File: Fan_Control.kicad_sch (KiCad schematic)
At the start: 6 parts, among them J20 Conn_01x03, J21 Conn_01x03

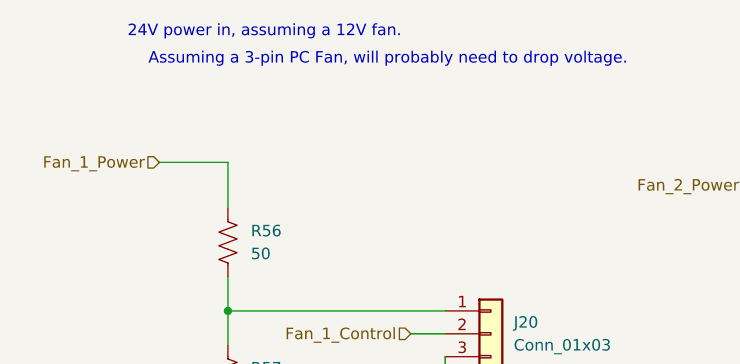
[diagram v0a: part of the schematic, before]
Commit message: Updated most of root-page labels.
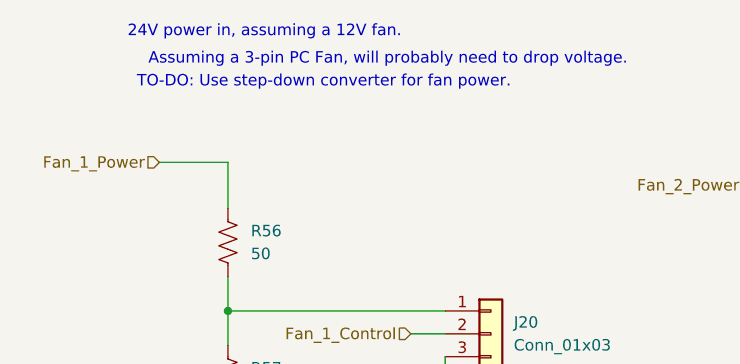
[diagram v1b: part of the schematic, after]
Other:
- note added: "TO-DO: Use step-down converter for fan power."
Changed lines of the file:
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@@
+		)
+	)
+	(text "TO-DO: Use step-down converter for fan power."
+		(exclude_from_sim no)
+		(at 67.818 82.55 0)
+		(effects
+			(font
+				(size 1.27 1.27)
+			)
 		)
 	)

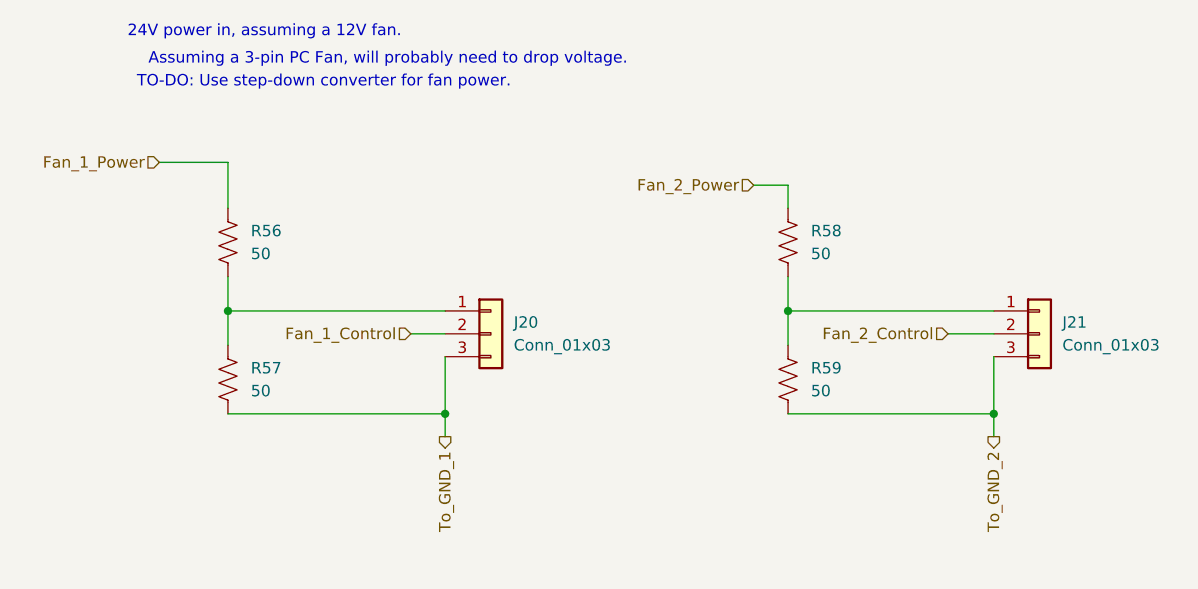
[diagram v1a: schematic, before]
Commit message: Added 24V-12V step-down converter for fans, started switch to devkit.
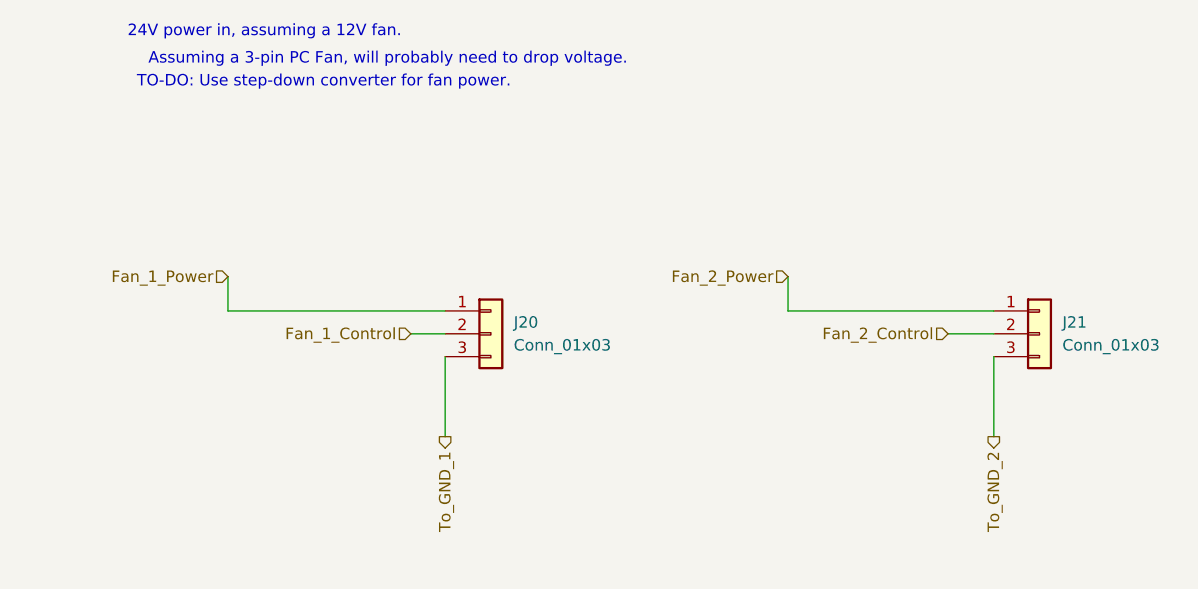
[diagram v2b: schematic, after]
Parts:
- removed R56, R57, R58, R59: 50, symbol Device:R_US
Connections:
- net Fan_1_Power: now also J20.1 (Pin_1)
- net Fan_2_Power: now also J21.1 (Pin_1)

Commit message: Updated to 4-pin fans, moved power pages together, deleted old reference.
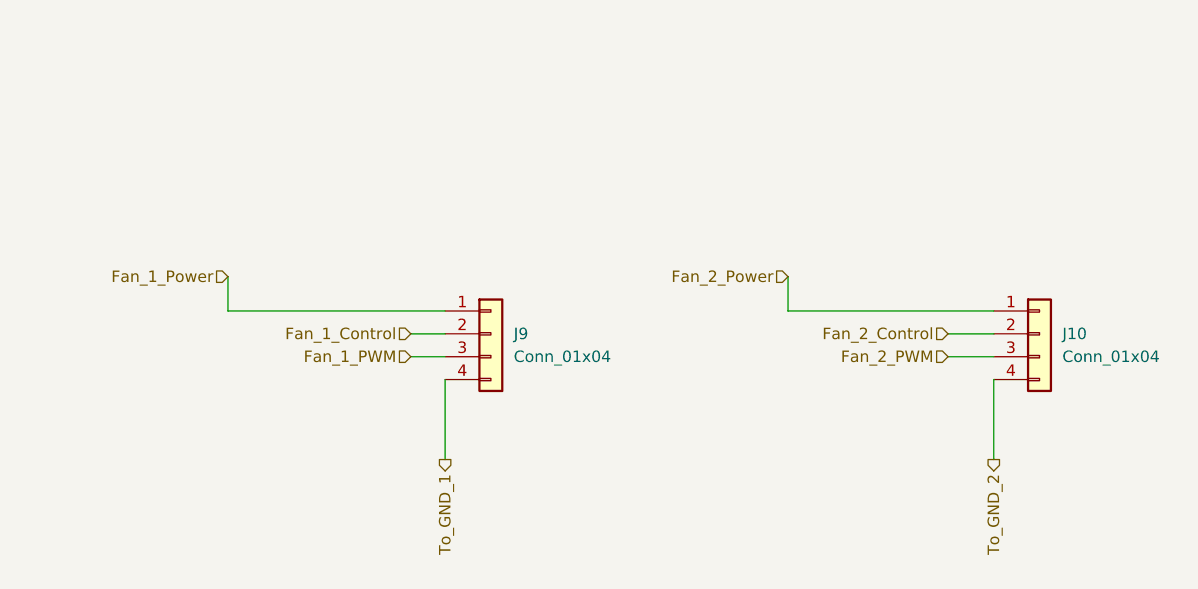
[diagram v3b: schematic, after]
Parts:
- removed J20, J21: Conn_01x03, symbol Connector_Generic:Conn_01x03
- added J10, J9: Conn_01x04, Connector_JST:JST_EH_B4B-EH-A_1x04_P2.50mm_Vertical, symbol Connector_Generic:Conn_01x04
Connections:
- net Fan_1_Control: now also J9.2 (Pin_2)
- net Fan_1_Power: now also J9.1 (Pin_1)
- net Fan_2_Control: now also J10.2 (Pin_2)
- net Fan_2_Power: now also J10.1 (Pin_1)
- net To_GND_1: now also J9.4 (Pin_4)
- net To_GND_2: now also J10.4 (Pin_4)
- new net Fan_1_PWM: J9.3 (Pin_3)
- new net Fan_2_PWM: J10.3 (Pin_3)
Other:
- note removed: "24V power in, assuming a 12V fan."
- note removed: "Assuming a 3-pin PC Fan, will probably need to drop voltage."
- note removed: "TO-DO: Use step-down converter for fan power."
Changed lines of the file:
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@@
 	(generator_version "9.0")
 	(paper "A4")
-	(text "24V power in, assuming a 12V fan."
-		(exclude_from_sim no)
-		(at 61.214 76.962 0)
-		(effects
-			(font
-				(size 1.27 1.27)
-			)
-		)
-	)
-	(text "TO-DO: Use step-down converter for fan power."
-		(exclude_from_sim no)
-		(at 67.818 82.55 0)
-		(effects
-			(font
-				(size 1.27 1.27)
-			)
-		)
-	)
-	(text "Assuming a 3-pin PC Fan, will probably need to drop voltage."
-		(exclude_from_sim no)
-		(at 74.93 80.01 0)
-		(effects
-			(font
-				(size 1.27 1.27)
-			)
-		)
-	)
-	(wire
-		(pts
-			(xy 142.24 113.03) (xy 142.24 121.92)
+	(wire
+		(pts
+			(xy 142.24 115.57) (xy 142.24 124.46)
 		)
 		(stroke
@@
 	(wire
 		(pts
-			(xy 81.28 113.03) (xy 81.28 121.92)
+			(xy 137.16 113.03) (xy 142.24 113.03)
+		)
+		(stroke
+			(width 0)
+			(type default)
+		)
+	)
+	(wire
+		(pts
+			(xy 81.28 115.57) (xy 81.28 124.46)
 		)
 		(stroke
@@
 	(wire
 		(pts
+			(xy 77.47 113.03) (xy 81.28 113.03)
+		)
+		(stroke
+			(width 0)
+			(type default)
+		)
+	)
+	(wire
+		(pts
 			(xy 57.15 104.14) (xy 57.15 107.95)
 		)
@@
 		(shape input)
 		(at 137.16 110.49 180)
+		(effects
+			(font
+				(size 1.27 1.27)
+			)
+			(justify right)
+		)
+	)
+	(hierarchical_label "Fan_1_PWM"
+		(shape input)
+		(at 77.47 113.03 180)
 		(effects
 			(font
@@
 	(hierarchical_label "To_GND_2"
 		(shape output)
-		(at 142.24 121.92 270)
+		(at 142.24 124.46 270)
 		(effects
 			(font
@@
 	(hierarchical_label "To_GND_1"
 		(shape output)
-		(at 81.28 121.92 270)
+		(at 81.28 124.46 270)
 		(effects
 			(font
@@
 		)
 	)
+	(hierarchical_label "Fan_2_PWM"
+		(shape input)
+		(at 137.16 113.03 180)
+		(effects
+			(font
+				(size 1.27 1.27)
+			)
+			(justify right)
+		)
+	)
 	(hierarchical_label "Fan_2_Power"
 		(shape input)
@@
 	)
 	(symbol
-		(lib_id "Connector_Generic:Conn_01x03")
+		(lib_id "Connector_Generic:Conn_01x04")
+		(at 86.36 110.49 0)
+		(unit 1)
+		(exclude_from_sim no)
+		(in_bom yes)
+		(on_board yes)
+		(dnp no)
+		(fields_autoplaced yes)
+		(property "Reference" "J9"
+			(at 88.9 110.4899 0)
+			(effects
+				(font
+					(size 1.27 1.27)
+				)
+				(justify left)
+			)
+		)
+		(property "Value" "Conn_01x04"
+			(at 88.9 113.0299 0)
+			(effects
+				(font
+					(size 1.27 1.27)
+				)
+				(justify left)
+			)
+		)
+		(property "Footprint" "Connector_JST:JST_EH_B4B-EH-A_1x04_P2.50mm_Vertical"
+			(at 86.36 110.49 0)
+			(effects
+				(font
+					(size 1.27 1.27)
+				)
+				(hide yes)
+			)
+		)
+		(property "Datasheet" "~"
+			(at 86.36 110.49 0)
+			(effects
+				(font
+					(size 1.27 1.27)
+				)
+				(hide yes)
+			)
+		)
+		(property "Description" "Generic connector, single row, 01x04, script generated (kicad-library-utils/schlib/autogen/connector/)"
+			(at 86.36 110.49 0)
+			(effects
+				(font
+					(size 1.27 1.27)
+				)
+				(hide yes)
+			)
+		)
+		(pin "3"
+		)
+		(pin "4"
+		)
+		(pin "2"
+		)
+		(pin "1"
+		)
+		(instances
+			(project ""
+				(path "/24817451-dfe0-4b9a-9d93-7304529c9d58/cec7ca12-a0bf-4031-9c0d-c0b354201f18"
+					(reference "J9")
+					(unit 1)
+				)
+			)
+		)
+	)
+	(symbol
+		(lib_id "Connector_Generic:Conn_01x04")
 		(at 147.32 110.49 0)
 		(unit 1)
@@
 		(dnp no)
 		(fields_autoplaced yes)
-		(property "Reference" "J21"
-			(at 149.86 109.2199 0)
+		(property "Reference" "J10"
+			(at 149.86 110.4899 0)
 			(effects
 				(font
@@
 			)
 		)
-		(property "Value" "Conn_01x03"
-			(at 149.86 111.7599 0)
+		(property "Value" "Conn_01x04"
+			(at 149.86 113.0299 0)
 			(effects
 				(font
@@
 			)
 		)
-		(property "Footprint" ""
+		(property "Footprint" "Connector_JST:JST_EH_B4B-EH-A_1x04_P2.50mm_Vertical"
 			(at 147.32 110.49 0)
 			(effects
@@
 			)
 		)
-		(property "Description" "Generic connector, single row, 01x03, script generated (kicad-library-utils/schlib/autogen/connector/)"
+		(property "Description" "Generic connector, single row, 01x04, script generated (kicad-library-utils/schlib/autogen/connector/)"
 			(at 147.32 110.49 0)
 			(effects
@@
 			)
 		)
+		(pin "3"
+		)
+		(pin "4"
+		)
 		(pin "2"
 		)
 		(pin "1"
-		)
-		(pin "3"
 		)
 		(instances
 			(project "QRET-ESP32"
 				(path "/24817451-dfe0-4b9a-9d93-7304529c9d58/cec7ca12-a0bf-4031-9c0d-c0b354201f18"
-					(reference "J21")
+					(reference "J10")
 					(unit 1)
 				)
-			)
-		)
-	)
-	(symbol
-		(lib_id "Connector_Generic:Conn_01x03")
-		(at 86.36 110.49 0)
-		(unit 1)
-		(exclude_from_sim no)
-		(in_bom yes)
-		(on_board yes)
-		(dnp no)
-		(fields_autoplaced yes)
-		(property "Reference" "J20"
-			(at 88.9 109.2199 0)
-			(effects
-				(font
-					(size 1.27 1.27)
-				)
-				(justify left)
-			)
-		)
-		(property "Value" "Conn_01x03"
-			(at 88.9 111.7599 0)
-			(effects
-				(font
-					(size 1.27 1.27)
-				)
-				(justify left)
-			)
-		)
-		(property "Footprint" ""
-			(at 86.36 110.49 0)
-			(effects
-				(font
-					(size 1.27 1.27)
-				)
-				(hide yes)
-			)
-		)
-		(property "Datasheet" "~"
-			(at 86.36 110.49 0)
-			(effects
-				(font
-					(size 1.27 1.27)
-				)
-				(hide yes)
-			)
-		)
-		(property "Description" "Generic connector, single row, 01x03, script generated (kicad-library-utils/schlib/autogen/connector/)"
-			(at 86.36 110.49 0)
-			(effects
-				(font
-					(size 1.27 1.27)
-				)
-				(hide yes)
-			)
-		)
-		(pin "2"
-		)
-		(pin "1"
-		)
-		(pin "3"
-		)
-		(instances
-			(project ""
-				(path "/24817451-dfe0-4b9a-9d93-7304529c9d58/cec7ca12-a0bf-4031-9c0d-c0b354201f18"
-					(reference "J20")
-					(unit 1)
-				)
